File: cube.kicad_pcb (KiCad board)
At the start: 2 copper layers, 300 parts, among them J1 serial_conn, J10 Conn_01x01, J11 Conn_01x01, J2 shifters_common_conn, J3 Conn_01x01, J4 Conn_01x01, J5 Conn_01x01, J6 Conn_01x01, J7 Conn_01x01, J8 Conn_01x01, J9 Conn_01x01, Q1 IRF9540N, Q2 IRF9540N, Q3 IRF9540N, Q4 IRF9540N, Q5 IRF9540N, Q6 IRF9540N, Q7 IRF9540N, Q8 IRF9540N, U1 SN74HC595N_0_b, U10 SN74HC595N_3_b, U11 SN74HC595N_3_g, U12 SN74HC595N_3_r, U13 SN74HC595N_4_b, U14 SN74HC595N_4_g, U15 SN74HC595N_4_r, U16 SN74HC595N_5_b, U17 SN74HC595N_5_g, U18 SN74HC595N_5_r, U19 SN74HC595N_6_b, U2 SN74HC595N_0_g, U20 SN74HC595N_6_g, U21 SN74HC595N_6_r, U22 SN74HC595N_7_b, U23 SN74HC595N_7_g, U24 SN74HC595N_7_r, U25 SN74HC595N_cols, U3 SN74HC595N_0_r, U4 SN74HC595N_1_b, U5 SN74HC595N_1_g, U6 SN74HC595N_1_r, U7 SN74HC595N_2_b, U8 SN74HC595N_2_g, U9 SN74HC595N_2_r

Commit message: fix 6th rows's blue conns
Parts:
- moved R121 3.04 mm to (197.9, 297.1), turned to 180 degrees
- moved R122 3.04 mm to (197.9, 267.1), turned to 180 degrees
- moved R123 3.04 mm to (197.9, 237.1), turned to 180 degrees
- moved R124 3.04 mm to (197.9, 207.1), turned to 180 degrees
- moved R125 3.04 mm to (197.9, 177.1), turned to 180 degrees
- moved R126 3.04 mm to (197.9, 147.1), turned to 180 degrees
- moved R127 3.04 mm to (197.9, 117.1), turned to 180 degrees
- moved R128 3.04 mm to (197.9, 87.1), turned to 180 degrees
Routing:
- net Net-(R127-Pad2): track 24.9 -> 18.3 mm
- net Net-(R128-Pad2): track 52.4 -> 45.8 mm
- net Net-(R123-Pad2): track 93.4 -> 98.0 mm
- net Net-(R125-Pad2): track 38.5 -> 43.0 mm
- net Net-(R124-Pad2): track 66.0 -> 70.5 mm
- net Net-(R121-Pad2): track 156.7 -> 161.3 mm
- net Net-(R122-Pad2): track 121.0 -> 125.4 mm
- net Net-(R126-Pad2): track 13.1 -> 15.6 mm
- net led_5_5_b: track 3.40 -> 2.10 mm
- net led_5_3_b: track 3.40 -> 2.10 mm
- net led_5_2_b: track 3.40 -> 2.10 mm
- net led_5_1_b: track 3.40 -> 2.10 mm
- net led_5_0_b: track 3.40 -> 2.10 mm
- net led_5_7_b: track 3.40 -> 2.10 mm
- net led_5_6_b: track 3.40 -> 2.10 mm

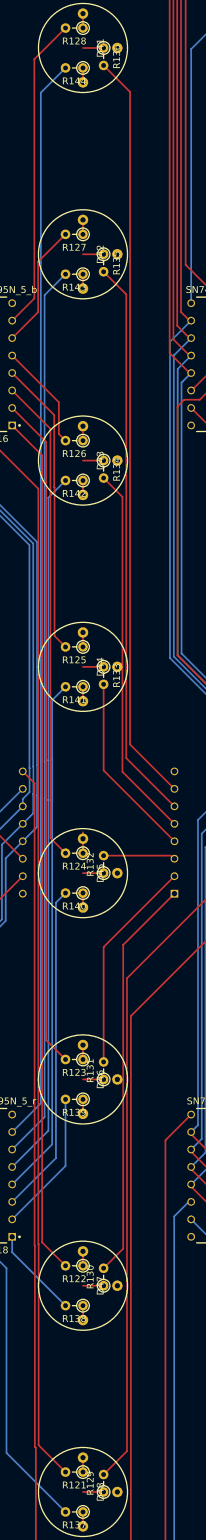
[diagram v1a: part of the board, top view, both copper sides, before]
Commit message: fix 6th rows's green conns
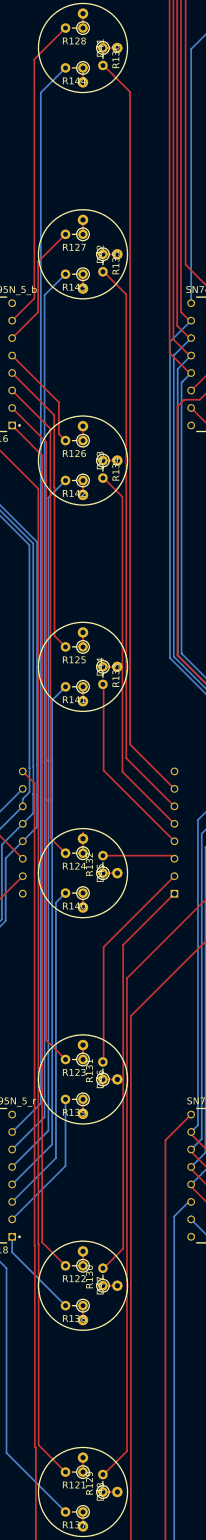
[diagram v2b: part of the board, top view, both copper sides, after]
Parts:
- moved R134 0.10 mm to (200.8, 150.0)
- moved R129 0.10 mm to (200.8, 300.0)
- moved R130 0.10 mm to (200.8, 270.0)
- moved R131 0.10 mm to (200.8, 240.0)
- moved R132 0.10 mm to (200.8, 210.0)
- moved R133 0.10 mm to (200.8, 180.0)
- moved R135 0.10 mm to (200.8, 120.0)
- moved R136 0.10 mm to (200.8, 90.0)
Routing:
- net led_5_7_g: track 3.00 -> 2.10 mm
- net led_5_6_g: track 3.00 -> 2.10 mm
- net led_5_5_g: track 3.00 -> 2.10 mm
- net led_5_4_g: track 3.00 -> 2.10 mm
- net led_5_3_g: track 3.00 -> 2.10 mm
- net led_5_2_g: track 3.00 -> 2.10 mm
- net led_5_1_g: track 3.00 -> 2.10 mm
- net led_5_0_g: track 3.00 -> 2.10 mm
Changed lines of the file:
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@@
   )
   (module Resistor_THT:R_Axial_DIN0204_L3.6mm_D1.6mm_P2.54mm_Vertical (layer F.Cu)
-    (at 200.940001 300 90)
+    (at 200.840001 300 90)
     (descr "Resistor, Axial_DIN0204 series, Axial, Vertical, pin pitch=2.54mm, 0.167W, length*diameter=3.6*1.6mm^2, http://cdn-reichelt.de/documents/datenblatt/B400/1_4W%23YAG.pdf")
     (tags "Resistor Axial_DIN0204 series Axial Vertical pin pitch 2.54mm 0.167W length 3.6mm diameter 1.6mm")
@@
   )
   (module Resistor_THT:R_Axial_DIN0204_L3.6mm_D1.6mm_P2.54mm_Vertical (layer F.Cu)
-    (at 200.940001 270 90)
+    (at 200.840001 270 90)
     (descr "Resistor, Axial_DIN0204 series, Axial, Vertical, pin pitch=2.54mm, 0.167W, length*diameter=3.6*1.6mm^2, http://cdn-reichelt.de/documents/datenblatt/B400/1_4W%23YAG.pdf")
     (tags "Resistor Axial_DIN0204 series Axial Vertical pin pitch 2.54mm 0.167W length 3.6mm diameter 1.6mm")
@@
   )
   (module Resistor_THT:R_Axial_DIN0204_L3.6mm_D1.6mm_P2.54mm_Vertical (layer F.Cu)
-    (at 200.940001 240 90)
+    (at 200.840001 240 90)
     (descr "Resistor, Axial_DIN0204 series, Axial, Vertical, pin pitch=2.54mm, 0.167W, length*diameter=3.6*1.6mm^2, http://cdn-reichelt.de/documents/datenblatt/B400/1_4W%23YAG.pdf")
     (tags "Resistor Axial_DIN0204 series Axial Vertical pin pitch 2.54mm 0.167W length 3.6mm diameter 1.6mm")
@@
   )
   (module Resistor_THT:R_Axial_DIN0204_L3.6mm_D1.6mm_P2.54mm_Vertical (layer F.Cu)
-    (at 200.94 210 90)
+    (at 200.84 210 90)
     (descr "Resistor, Axial_DIN0204 series, Axial, Vertical, pin pitch=2.54mm, 0.167W, length*diameter=3.6*1.6mm^2, http://cdn-reichelt.de/documents/datenblatt/B400/1_4W%23YAG.pdf")
     (tags "Resistor Axial_DIN0204 series Axial Vertical pin pitch 2.54mm 0.167W length 3.6mm diameter 1.6mm")
@@
   )
   (module Resistor_THT:R_Axial_DIN0204_L3.6mm_D1.6mm_P2.54mm_Vertical (layer F.Cu)
-    (at 200.94 180 270)
+    (at 200.84 180 270)
     (descr "Resistor, Axial_DIN0204 series, Axial, Vertical, pin pitch=2.54mm, 0.167W, length*diameter=3.6*1.6mm^2, http://cdn-reichelt.de/documents/datenblatt/B400/1_4W%23YAG.pdf")
     (tags "Resistor Axial_DIN0204 series Axial Vertical pin pitch 2.54mm 0.167W length 3.6mm diameter 1.6mm")
@@
   )
   (module Resistor_THT:R_Axial_DIN0204_L3.6mm_D1.6mm_P2.54mm_Vertical (layer F.Cu)
-    (at 200.94 149.999999 270)
+    (at 200.84 150 270)
     (descr "Resistor, Axial_DIN0204 series, Axial, Vertical, pin pitch=2.54mm, 0.167W, length*diameter=3.6*1.6mm^2, http://cdn-reichelt.de/documents/datenblatt/B400/1_4W%23YAG.pdf")
     (tags "Resistor Axial_DIN0204 series Axial Vertical pin pitch 2.54mm 0.167W length 3.6mm diameter 1.6mm")
@@
   )
   (module Resistor_THT:R_Axial_DIN0204_L3.6mm_D1.6mm_P2.54mm_Vertical (layer F.Cu)
-    (at 200.94 120 270)
+    (at 200.84 120 270)
     (descr "Resistor, Axial_DIN0204 series, Axial, Vertical, pin pitch=2.54mm, 0.167W, length*diameter=3.6*1.6mm^2, http://cdn-reichelt.de/documents/datenblatt/B400/1_4W%23YAG.pdf")
     (tags "Resistor Axial_DIN0204 series Axial Vertical pin pitch 2.54mm 0.167W length 3.6mm diameter 1.6mm")
@@
   )
   (module Resistor_THT:R_Axial_DIN0204_L3.6mm_D1.6mm_P2.54mm_Vertical (layer F.Cu)
-    (at 200.94 90 270)
+    (at 200.84 90 270)
     (descr "Resistor, Axial_DIN0204 series, Axial, Vertical, pin pitch=2.54mm, 0.167W, length*diameter=3.6*1.6mm^2, http://cdn-reichelt.de/documents/datenblatt/B400/1_4W%23YAG.pdf")
     (tags "Resistor Axial_DIN0204 series Axial Vertical pin pitch 2.54mm 0.167W length 3.6mm diameter 1.6mm")
@@
   (segment (start 177.927 246.5272) (end 177.927 311.2008) (width 0.25) (layer B.Cu) (net 339))
   (segment (start 197.94 95) (end 197.94 92.9) (width 0.25) (layer F.Cu) (net 340))
-  (segment (start 200.94 90) (end 197.94 90) (width 0.25) (layer F.Cu) (net 341))
+  (segment (start 202.94 90) (end 200.84 90) (width 0.25) (layer F.Cu) (net 341))
   (segment (start 197.94 87.1) (end 197.94 85) (width 0.25) (layer F.Cu) (net 342))
   (segment (start 197.94 125) (end 197.94 122.9) (width 0.25) (layer F.Cu) (net 343))
-  (segment (start 200.94 120) (end 197.94 120) (width 0.25) (layer F.Cu) (net 344))
+  (segment (start 202.94 120) (end 200.84 120) (width 0.25) (layer F.Cu) (net 344))
   (segment (start 197.94 117.1) (end 197.94 115) (width 0.25) (layer F.Cu) (net 345))
   (segment (start 197.94 155) (end 197.94 152.9) (width 0.25) (layer F.Cu) (net 346))
-  (segment (start 200.94 150) (end 197.94 150) (width 0.25) (layer F.Cu) (net 347))
+  (segment (start 202.94 150) (end 200.84 150) (width 0.25) (layer F.Cu) (net 347))
   (segment (start 197.94 147.1) (end 197.94 145) (width 0.25) (layer F.Cu) (net 348))
   (segment (start 197.94 185) (end 197.94 182.9) (width 0.25) (layer F.Cu) (net 349))
-  (segment (start 200.94 180) (end 197.94 180) (width 0.25) (layer F.Cu) (net 350))
+  (segment (start 202.94 180) (end 200.84 180) (width 0.25) (layer F.Cu) (net 350))
   (segment (start 197.94 177.1) (end 197.94 175) (width 0.25) (layer F.Cu) (net 351))
   (segment (start 197.94 215) (end 197.94 212.9) (width 0.25) (layer F.Cu) (net 352))
-  (segment (start 200.94 210) (end 197.94 210) (width 0.25) (layer F.Cu) (net 353))
+  (segment (start 202.94 210) (end 200.84 210) (width 0.25) (layer F.Cu) (net 353))
   (segment (start 197.94 207.46) (end 197.94 204.06) (width 0.25) (layer F.Cu) (net 354))
   (segment (start 197.940001 245) (end 197.940001 242.9) (width 0.25) (layer F.Cu) (net 355))
-  (segment (start 200.94 240) (end 197.94 240) (width 0.25) (layer F.Cu) (net 356))
+  (segment (start 202.940001 240) (end 200.840001 240) (width 0.25) (layer F.Cu) (net 356))
   (segment (start 197.940001 237.1) (end 197.940001 235) (width 0.25) (layer F.Cu) (net 357))
   (segment (start 197.940001 275) (end 197.940001 272.9) (width 0.25) (layer F.Cu) (net 358))
-  (segment (start 200.94 270) (end 197.94 270) (width 0.25) (layer F.Cu) (net 359))
+  (segment (start 202.940001 270) (end 200.840001 270) (width 0.25) (layer F.Cu) (net 359))
   (segment (start 197.940001 267.1) (end 197.940001 265) (width 0.25) (layer F.Cu) (net 360))
   (segment (start 197.940001 305) (end 197.940001 302.9) (width 0.25) (layer F.Cu) (net 361))
-  (segment (start 200.94 300) (end 197.94 300) (width 0.25) (layer F.Cu) (net 362))
+  (segment (start 202.940001 300) (end 200.840001 300) (width 0.25) (layer F.Cu) (net 362))
   (segment (start 197.940001 297.1) (end 197.940001 295) (width 0.25) (layer F.Cu) (net 363))
   (segment (start 231.909999 87.46) (end 231.909999 84.06) (width 0.25) (layer F.Cu) (net 364))

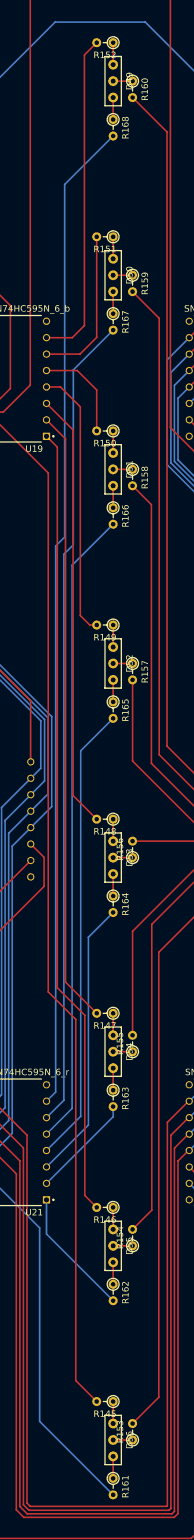
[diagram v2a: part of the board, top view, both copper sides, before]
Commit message: fix 7th rows's red conns
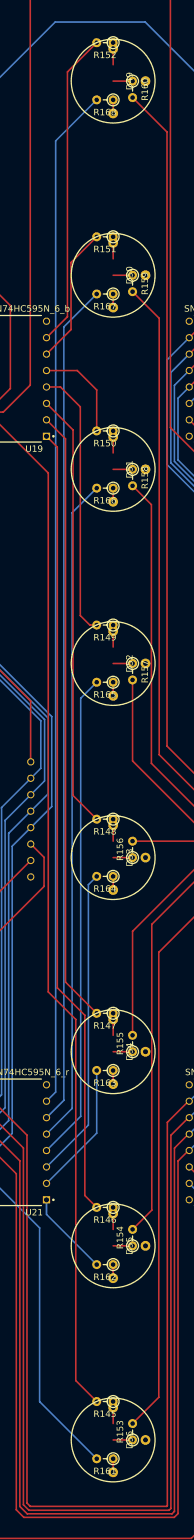
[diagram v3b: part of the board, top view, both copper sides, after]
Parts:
- moved R161 3.04 mm to (231.9, 302.9), turned to 180 degrees
- moved R162 3.04 mm to (231.9, 272.9), turned to 180 degrees
- moved R163 3.04 mm to (231.9, 242.9), turned to 180 degrees
- moved R164 3.04 mm to (231.9, 212.9), turned to 180 degrees
- moved R165 3.04 mm to (231.9, 182.9), turned to 180 degrees
- moved R166 3.04 mm to (231.9, 152.9), turned to 180 degrees
- moved R167 3.04 mm to (231.9, 122.9), turned to 180 degrees
- moved R168 3.04 mm to (231.9, 92.9), turned to 180 degrees
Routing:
- net Net-(R162-Pad2): track 19.9 -> 13.2 mm
- net Net-(R161-Pad2): track 55.7 -> 49.1 mm
- net Net-(R164-Pad2): track 43.6 -> 48.1 mm
- net Net-(R163-Pad2): track 16.1 -> 20.7 mm
- net Net-(R166-Pad2): track 98.5 -> 103.0 mm
- net Net-(R165-Pad2): track 71.1 -> 75.6 mm
- net Net-(R168-Pad2): track 153.4 -> 158.0 mm
- net Net-(R167-Pad2): track 126.0 -> 130.5 mm
- net Net-(R151-Pad2): track 24.4 -> 21.3 mm
- net Net-(R152-Pad2): track 51.1 -> 48.8 mm
- net led_6_5_r: track 3.40 -> 2.10 mm
- net led_6_4_r: track 3.40 -> 2.10 mm
- net led_6_3_r: track 3.40 -> 2.10 mm
- net led_6_2_r: track 3.40 -> 2.10 mm
- net led_6_1_r: track 3.40 -> 2.10 mm
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
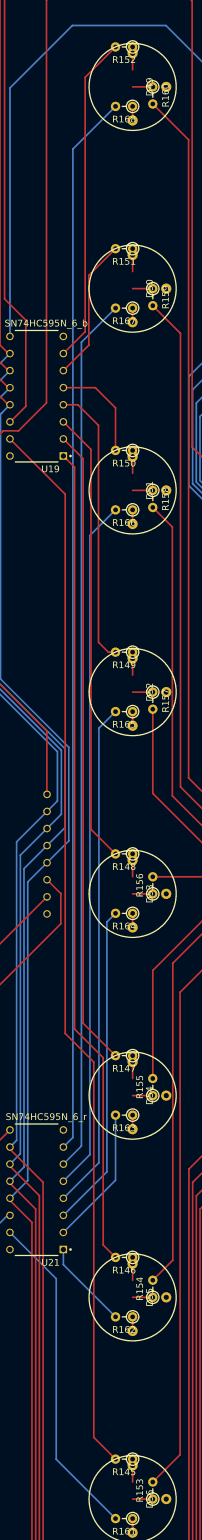
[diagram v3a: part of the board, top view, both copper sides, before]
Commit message: fix 7th rows's blue conns
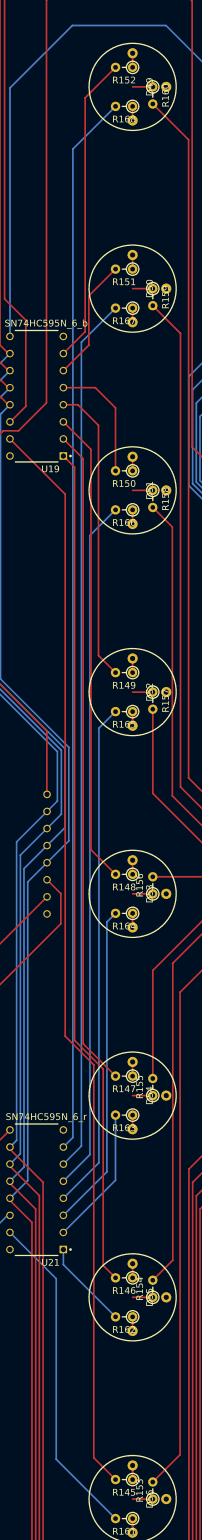
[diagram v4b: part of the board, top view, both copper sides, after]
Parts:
- moved R148 3.04 mm to (231.9, 207.1)
- moved R151 3.04 mm to (231.9, 117.1)
- moved R145 3.04 mm to (231.9, 297.1)
- moved R146 3.04 mm to (231.9, 267.1)
- moved R147 3.04 mm to (231.9, 237.1)
- moved R149 3.04 mm to (231.9, 177.1)
- moved R150 3.04 mm to (231.9, 147.1)
- moved R152 3.04 mm to (231.9, 87.1)
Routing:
- net Net-(R145-Pad2): track 158.3 -> 161.4 mm
- net Net-(R147-Pad2): track 94.9 -> 98.0 mm
- net Net-(R148-Pad2): track 67.5 -> 70.5 mm
- net Net-(R146-Pad2): track 122.4 -> 125.4 mm
- net Net-(R150-Pad2): track 15.3 -> 18.4 mm
- net Net-(R152-Pad2): track 48.8 -> 45.8 mm
- net Net-(R151-Pad2): track 21.3 -> 18.3 mm
- net Net-(R149-Pad2): track 41.9 -> 44.3 mm
- net led_6_5_b: track 3.40 -> 2.10 mm
- net led_6_4_b: track 3.40 -> 2.10 mm
- net led_6_3_b: track 3.40 -> 2.10 mm
- net led_6_2_b: track 3.40 -> 2.10 mm
- net led_6_1_b: track 3.40 -> 2.10 mm
- net led_6_0_b: track 3.40 -> 2.10 mm
- net led_6_7_b: track 3.40 -> 2.10 mm
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
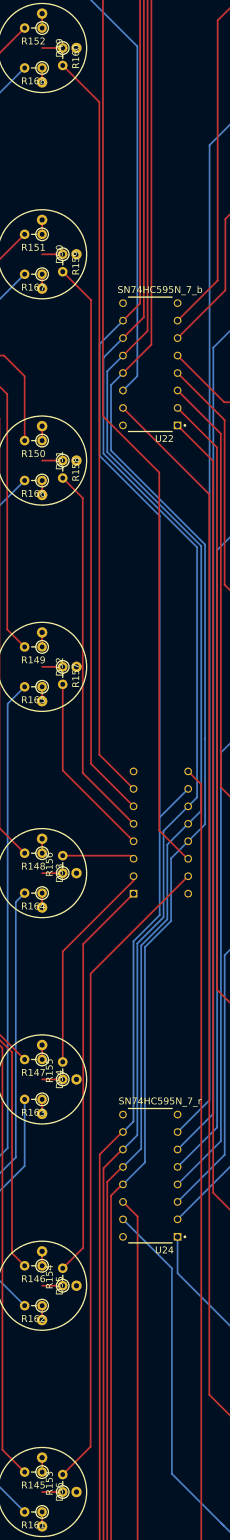
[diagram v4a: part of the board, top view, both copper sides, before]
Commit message: fix 7th rows's green conns
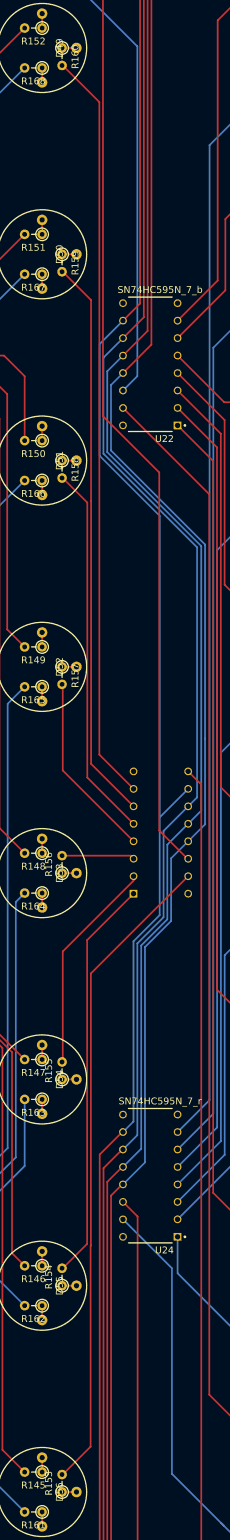
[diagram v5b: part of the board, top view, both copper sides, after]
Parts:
- moved R160 0.10 mm to (234.8, 90.0)
- moved R153 0.10 mm to (234.8, 300.0)
- moved R154 0.10 mm to (234.8, 270.0)
- moved R155 0.10 mm to (234.8, 240.0)
- moved R156 0.10 mm to (234.8, 210.0)
- moved R157 0.10 mm to (234.8, 180.0)
- moved R158 0.10 mm to (234.8, 150.0)
- moved R159 0.10 mm to (234.8, 120.0)
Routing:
- net led_6_7_g: track 3.00 -> 2.10 mm
- net led_6_6_g: track 3.00 -> 2.10 mm
- net led_6_5_g: track 3.00 -> 2.10 mm
- net led_6_4_g: track 3.00 -> 2.10 mm
- net led_6_3_g: track 3.00 -> 2.10 mm
- net led_6_2_g: track 3.00 -> 2.10 mm
- net led_6_1_g: track 3.00 -> 2.10 mm
- net led_6_0_g: track 3.00 -> 2.10 mm

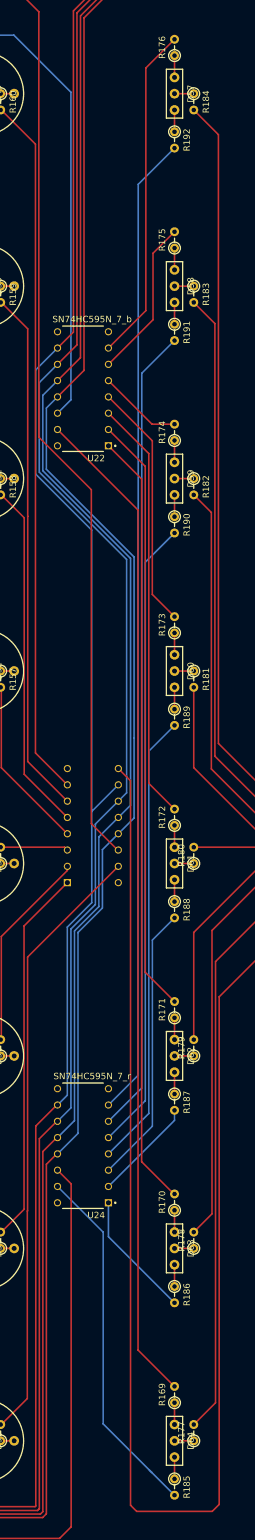
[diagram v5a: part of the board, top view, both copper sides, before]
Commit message: fix 8th rows's red conns
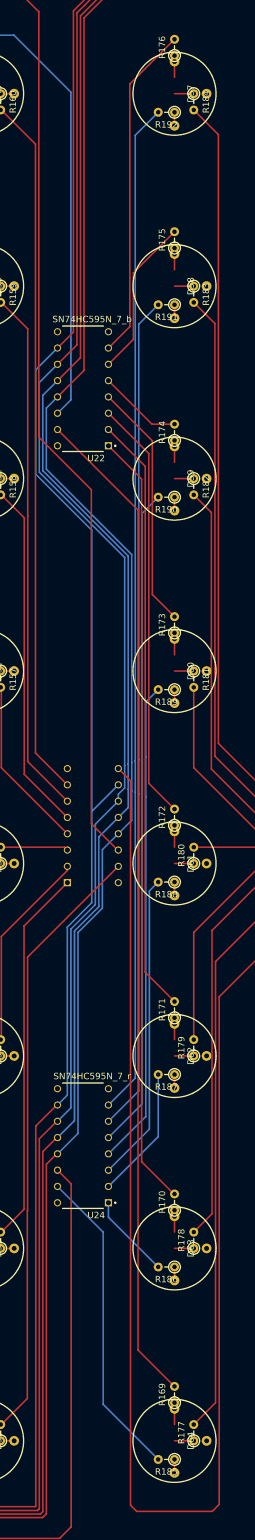
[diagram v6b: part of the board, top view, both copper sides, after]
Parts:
- moved R185 3.04 mm to (261.9, 302.9), turned to 180 degrees
- moved R186 3.04 mm to (261.9, 272.9), turned to 180 degrees
- moved R187 3.04 mm to (261.9, 242.9), turned to 180 degrees
- moved R188 3.04 mm to (261.9, 212.9), turned to 180 degrees
- moved R189 3.04 mm to (261.9, 182.9), turned to 180 degrees
- moved R190 3.04 mm to (261.9, 152.9), turned to 180 degrees
- moved R191 3.04 mm to (261.9, 122.9), turned to 180 degrees
- moved R192 3.04 mm to (261.9, 92.9), turned to 180 degrees
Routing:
- net Net-(R185-Pad2): track 56.3 -> 49.1 mm
- net Net-(R186-Pad2): track 19.9 -> 13.2 mm
- net Net-(R191-Pad2): track 126.0 -> 130.5 mm
- net Net-(R189-Pad2): track 71.1 -> 75.6 mm
- net Net-(R192-Pad2): track 153.4 -> 158.0 mm
- net Net-(R190-Pad2): track 98.5 -> 103.0 mm
- net Net-(R187-Pad2): track 16.1 -> 20.7 mm
- net Net-(R188-Pad2): track 43.6 -> 48.1 mm
- net led_7_5_r: track 3.40 -> 2.10 mm
- net led_7_4_r: track 3.40 -> 2.10 mm
- net led_7_3_r: track 3.40 -> 2.10 mm
- net led_7_2_r: track 3.40 -> 2.10 mm
- net led_7_1_r: track 3.40 -> 2.10 mm
- net led_7_0_r: track 3.40 -> 2.10 mm
- net led_7_7_r: track 3.40 -> 2.10 mm
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
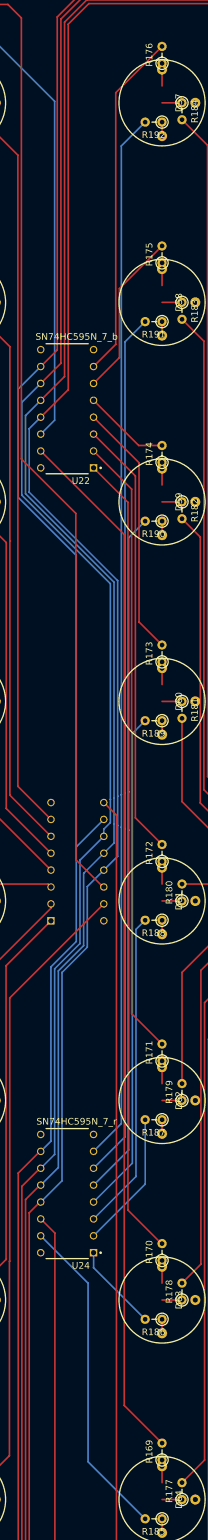
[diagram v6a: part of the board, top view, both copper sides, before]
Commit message: fix 8th rows's blue conns
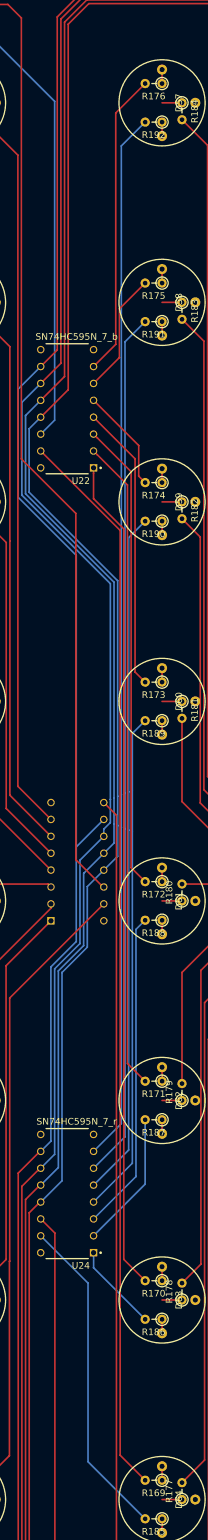
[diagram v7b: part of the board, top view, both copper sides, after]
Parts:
- moved R169 3.04 mm to (261.9, 297.1), turned to 180 degrees
- moved R170 3.04 mm to (261.9, 267.1), turned to 180 degrees
- moved R171 3.04 mm to (261.9, 237.1), turned to 180 degrees
- moved R172 3.04 mm to (261.9, 207.1), turned to 180 degrees
- moved R173 3.04 mm to (261.9, 177.1), turned to 180 degrees
- moved R174 3.04 mm to (261.9, 147.1), turned to 180 degrees
- moved R175 3.04 mm to (261.9, 117.1), turned to 180 degrees
- moved R176 3.04 mm to (261.9, 87.1), turned to 180 degrees
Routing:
- net Net-(R175-Pad2): track 24.9 -> 18.3 mm
- net Net-(R176-Pad2): track 52.4 -> 45.8 mm
- net Net-(R171-Pad2): track 93.4 -> 98.0 mm
- net Net-(R172-Pad2): track 66.0 -> 70.5 mm
- net Net-(R173-Pad2): track 38.5 -> 43.0 mm
- net Net-(R169-Pad2): track 156.7 -> 161.3 mm
- net Net-(R170-Pad2): track 121.0 -> 125.4 mm
- net Net-(R174-Pad2): track 13.1 -> 15.6 mm
- net led_7_5_b: track 3.40 -> 2.10 mm
- net led_7_4_b: track 3.40 -> 2.10 mm
- net led_7_3_b: track 3.40 -> 2.10 mm
- net led_7_2_b: track 3.40 -> 2.10 mm
- net led_7_1_b: track 3.40 -> 2.10 mm
- net led_7_0_b: track 3.40 -> 2.10 mm
- net led_7_7_b: track 3.40 -> 2.10 mm
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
